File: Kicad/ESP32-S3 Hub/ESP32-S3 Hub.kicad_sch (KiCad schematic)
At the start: 26 parts, among them U1 ESP32-S3, Y1 ABM11-40.000MHZ-B1U-T3, 10ppm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

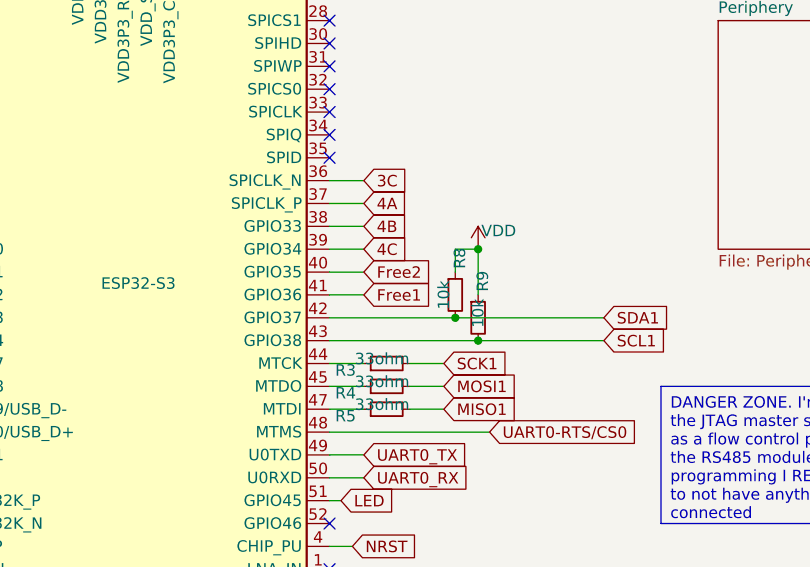
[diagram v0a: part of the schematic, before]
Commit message: Swapped header logical numbers
I realized my numbering scheme was off with the actual board layout. So in the schematic I swapped the connectors without rewiring so that the numbers are more logical. CS7, CS8, and Free2 are now for the top mezzanine connector, which is closer to the pins on the chips. It also falls in line with my bottom up numbering scheme.
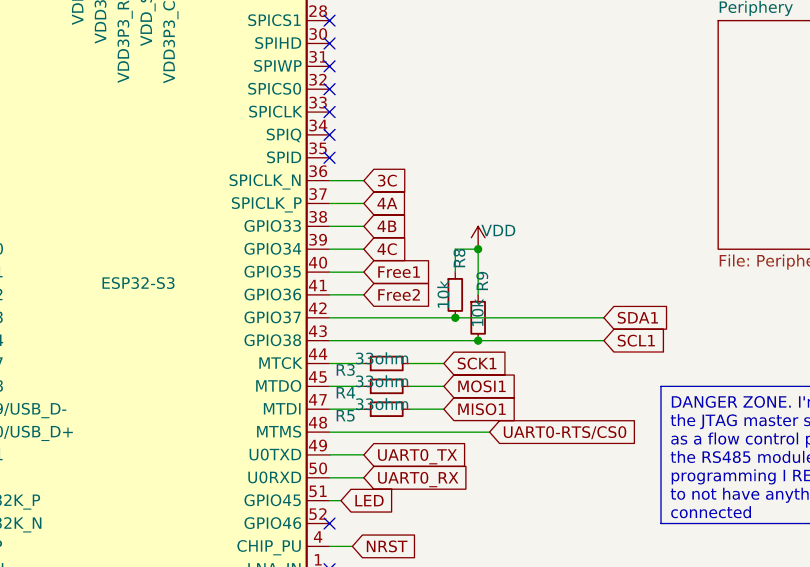
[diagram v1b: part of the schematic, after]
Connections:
- net Free1: now also U1.40 (GPIO35); no longer U1.41 (GPIO36)
- net Free2: now also U1.41 (GPIO36); no longer U1.40 (GPIO35)

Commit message: Routed Free 1 and 2 pins
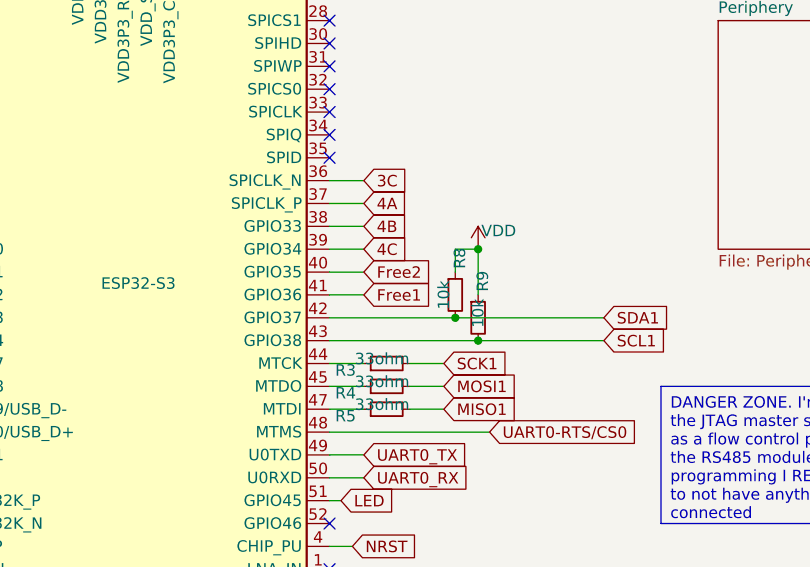
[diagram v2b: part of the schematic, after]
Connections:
- net Free1: now also U1.41 (GPIO36); no longer U1.40 (GPIO35)
- net Free2: now also U1.40 (GPIO35); no longer U1.41 (GPIO36)
